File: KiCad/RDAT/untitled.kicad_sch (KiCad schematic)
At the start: 10 parts, among them M1 Fan_4pin

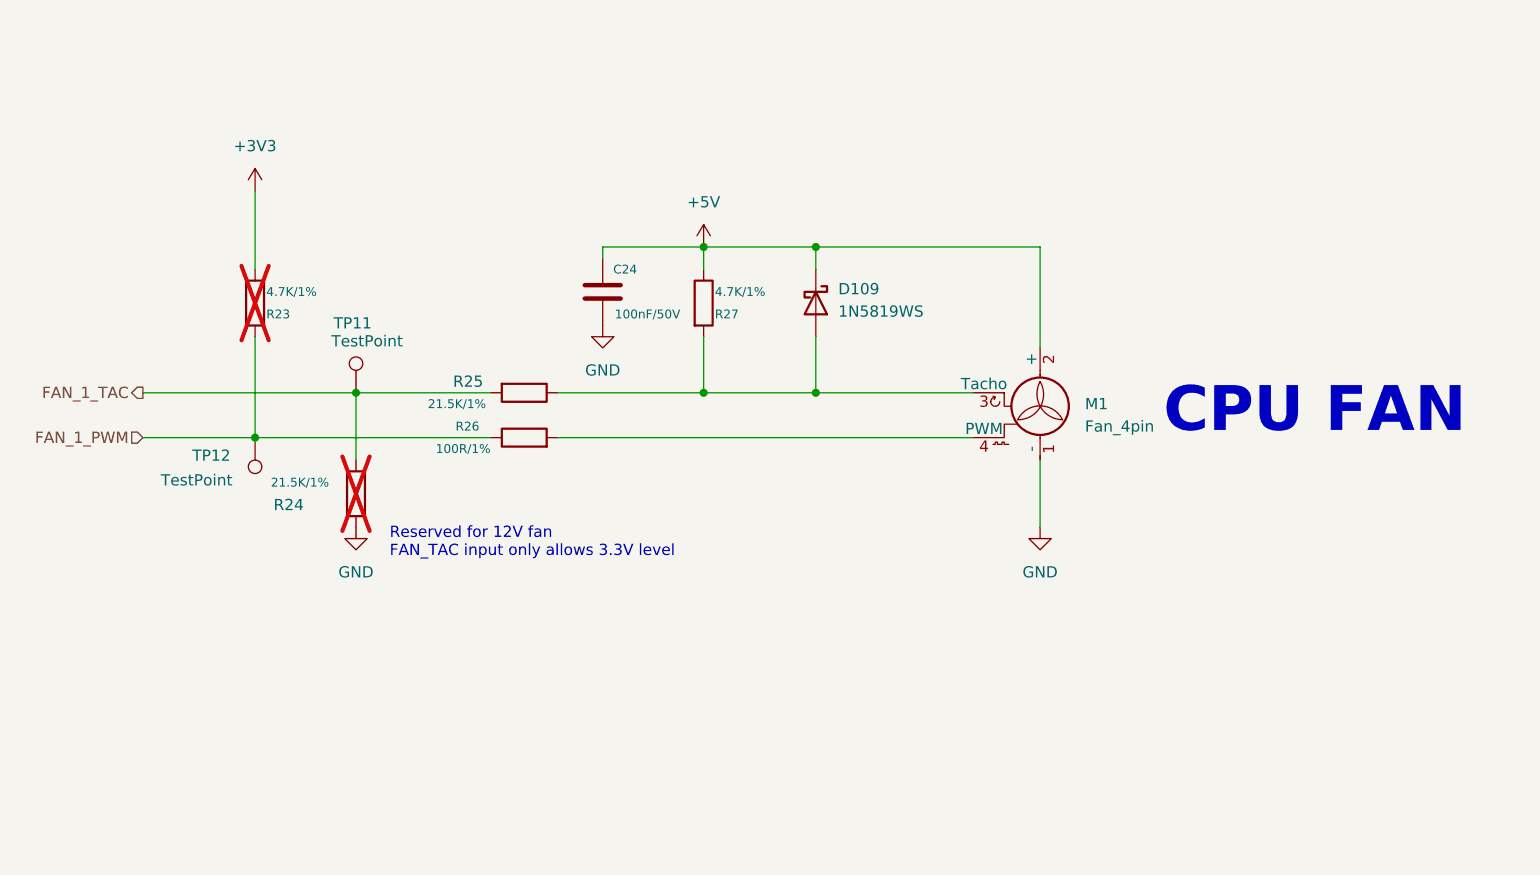
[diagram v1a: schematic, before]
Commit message: Added Libs and DOCS
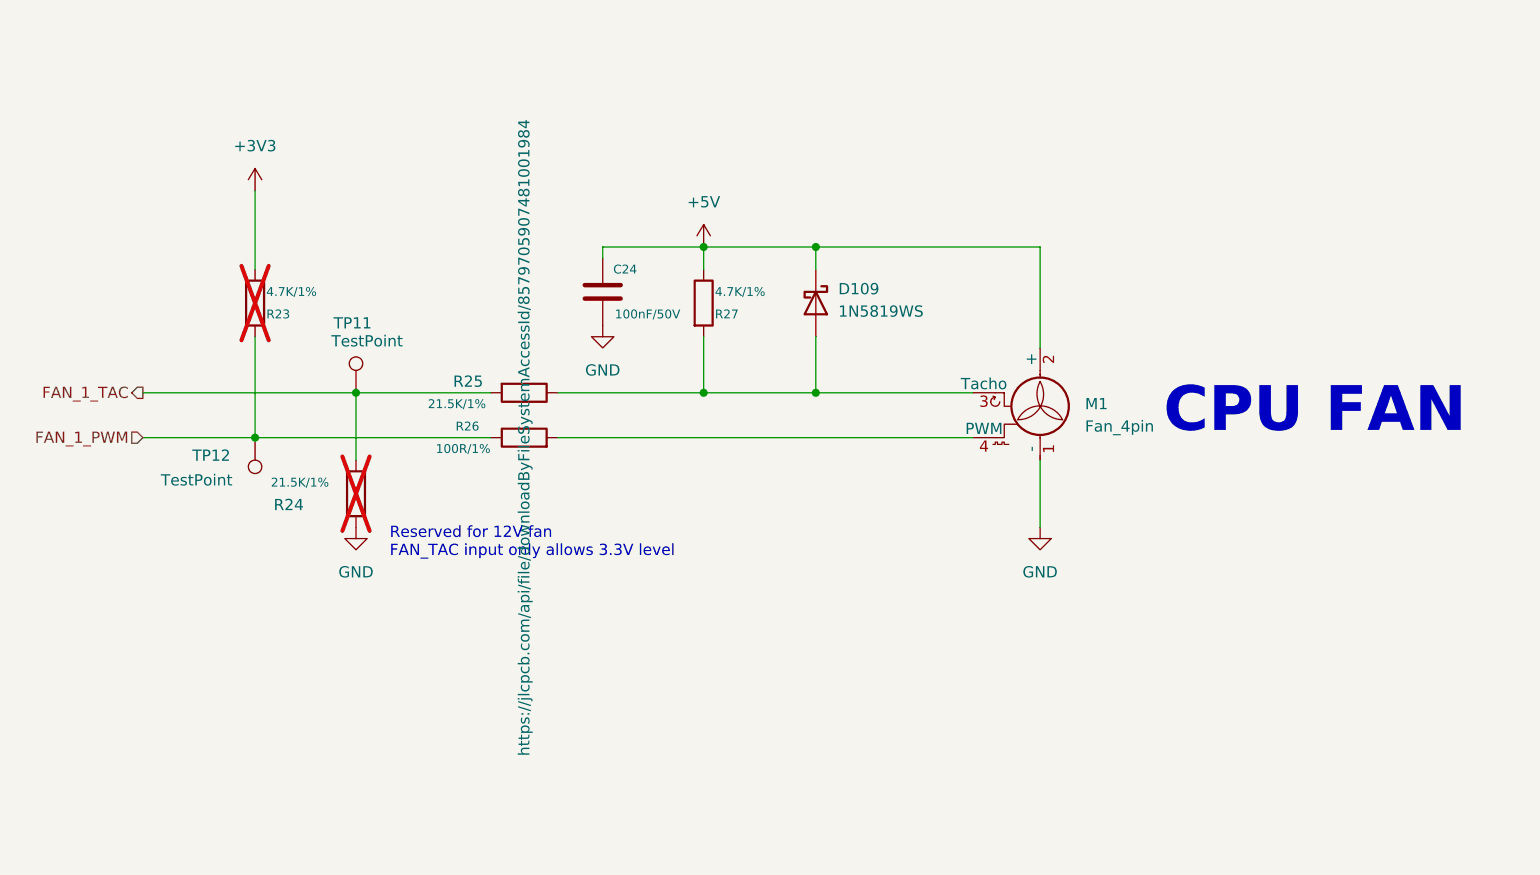
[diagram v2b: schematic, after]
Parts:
- M1: JLCPCB_LINK (none) -> https://jlcpcb.com/partdetail/Jst-B4B_PH_K_K_LF_SN/C5305780
- R26: JLCPCB_LINK (none) -> https://jlcpcb.com/api/file/downloadByFileSystemAccessId/85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
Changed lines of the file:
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@@
 			)
 		)
-		(property "Datasheet" "~"
+		(property "Datasheet" "https://jlcpcb.com/partdetail/25819-0402WGF1000TCE/C25076"
 			(at 139.7 93.98 0)
 			(effects
@@
 			)
 		)
-		(property "JLCPCB_LINK" ""
+		(property "JLCPCB_LINK" "https://jlcpcb.com/api/file/downloadByFileSystemAccessId/8579705907481001984"
 			(at 139.7 93.98 0)
 			(effects
@@
 			)
 		)
-		(property "JLCPCB_LINK" ""
+		(property "JLCPCB_LINK" "https://jlcpcb.com/partdetail/Jst-B4B_PH_K_K_LF_SN/C5305780"
 			(at 198.12 91.44 0)
 			(effects
@@
 					(size 1.27 1.27)
 				)
-			)
-		)
+				(hide yes)
+			)
+		)

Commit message: Sourced and documented all parts
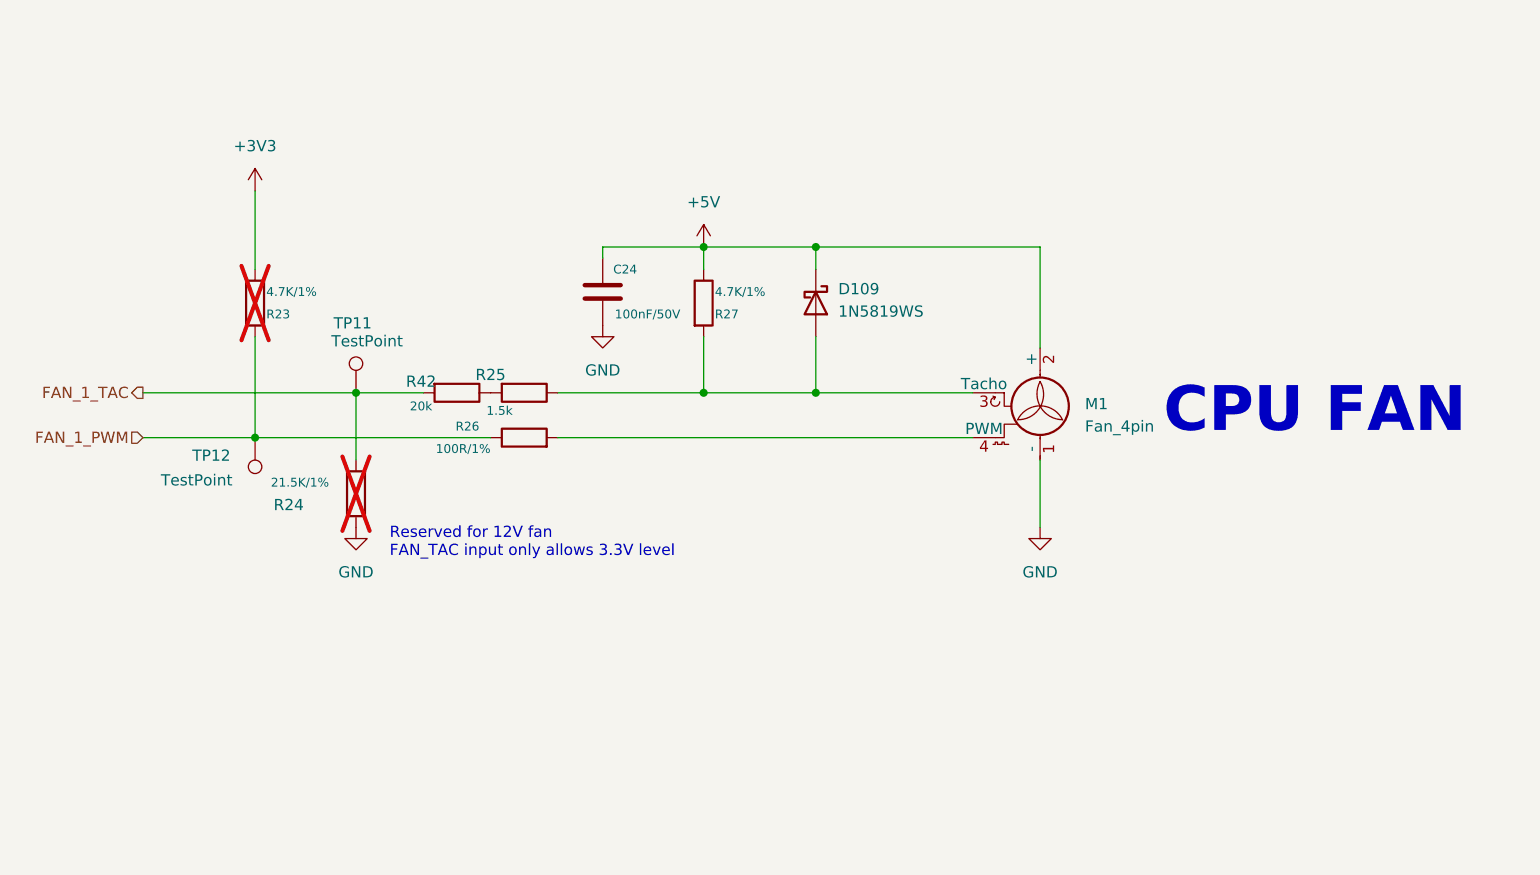
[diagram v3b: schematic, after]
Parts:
- added R42: 20k, A_HDJ_Library:R_0402_1005Metric, symbol Device:R
- C24: JLCPCB_LINK (none) -> https://jlcpcb.com/partdetail/291005-CL05B104KB54PNC/C307331
- D109: JLCPCB_LINK (none) -> https://jlcpcb.com/partdetail/GuangdongHottech-1N5819WS/C19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
- R25: value 21.5K/1% -> 1.5k; JLCPCB_LINK (none) -> https://jlcpcb.com/partdetail/26610-0402WGF1501TCE/C25867
- R26: JLCPCB_LINK https://jlcpcb.com/api/file/downloadByFileSystemAccessId/85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 -> https://jlcpcb.com/partdetail/25819-0402WGF1000TCE/C25076
- R27: JLCPCB_LINK (none) -> https://jlcpcb.com/partdetail/26643-0402WGF4701TCE/C25900
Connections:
- net FAN_1_TAC: now also R42.2; no longer R25.2
- new net: R25.2, R42.1
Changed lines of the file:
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@@
 	(wire
 		(pts
-			(xy 120.65 88.9) (xy 135.89 88.9)
+			(xy 120.65 88.9) (xy 128.27 88.9)
 		)
 		(stroke
@@
 			)
 		)
-		(property "Datasheet" "https://jlcpcb.com/partdetail/25819-0402WGF1000TCE/C25076"
+		(property "Datasheet" "https://jlcpcb.com/api/file/downloadByFileSystemAccessId/8579705907481001984"
 			(at 139.7 93.98 0)
 			(effects
@@
 			)
 		)
-		(property "JLCPCB_LINK" "https://jlcpcb.com/api/file/downloadByFileSystemAccessId/8579705907481001984"
+		(property "JLCPCB_LINK" "https://jlcpcb.com/partdetail/25819-0402WGF1000TCE/C25076"
 			(at 139.7 93.98 0)
 			(effects
@@
 					(size 1.27 1.27)
 				)
+				(hide yes)
 			)
 		)
@@
 			)
 		)
-		(property "Datasheet" "~"
+		(property "Datasheet" "https://jlcpcb.com/api/file/downloadByFileSystemAccessId/8554627388281098240"
 			(at 148.59 77.47 0)
 			(effects
@@
 			)
 		)
-		(property "JLCPCB_LINK" ""
+		(property "JLCPCB_LINK" "https://jlcpcb.com/partdetail/291005-CL05B104KB54PNC/C307331"
 			(at 148.59 77.47 0)
 			(effects
@@
 					(size 1.27 1.27)
 				)
+				(hide yes)
 			)
 		)
@@
 	)
 	(symbol
+		(lib_id "Device:R")
+		(at 132.08 88.9 270)
+		(unit 1)
+		(exclude_from_sim no)
+		(in_bom yes)
+		(on_board yes)
+		(dnp no)
+		(property "Reference" "R42"
+			(at 128.016 87.63 90)
+			(effects
+				(font
+					(size 1.27 1.27)
+				)
+			)
+		)
+		(property "Value" "20k"
+			(at 128.016 90.424 90)
+			(effects
+				(font
+					(size 1 1)
+				)
+			)
+		)
+		(property "Footprint" "A_HDJ_Library:R_0402_1005Metric"
+			(at 132.08 87.122 90)
+			(effects
+				(font
+					(size 1.27 1.27)
+				)
+				(hide yes)
+			)
+		)
+		(property "Datasheet" "https://jlcpcb.com/api/file/downloadByFileSystemAccessId/8579705988980932608"
+			(at 132.08 88.9 0)
+			(effects
+				(font
+					(size 1.27 1.27)
+				)
+				(hide yes)
+			)
+		)
+		(property "Description" ""
+			(at 132.08 88.9 0)
+			(effects
+				(font
+					(size 1.27 1.27)
+				)
+				(hide yes)
+			)
+		)
+		(property "SCH_Show_Footprint" ""
+			(at 132.08 88.9 0)
+			(effects
+				(font
+					(size 1.27 1.27)
+				)
+				(hide yes)
+			)
+		)
+		(property "Sim.Device" ""
+			(at 132.08 88.9 0)
+			(effects
+				(font
+					(size 1.27 1.27)
+				)
+				(hide yes)
+			)
+		)
+		(property "Sim.Pins" ""
+			(at 132.08 88.9 0)
+			(effects
+				(font
+					(size 1.27 1.27)
+				)
+				(hide yes)
+			)
+		)
+		(property "Sim.Type" ""
+			(at 132.08 88.9 0)
+			(effects
+				(font
+					(size 1.27 1.27)
+				)
+				(hide yes)
+			)
+		)
+		(property "JLCPCB_LINK" "https://jlcpcb.com/partdetail/26508-0402WGF2002TCE/C25765"
+			(at 132.08 88.9 0)
+			(effects
+				(font
+					(size 1.27 1.27)
+				)
+				(hide yes)
+			)
+		)
+		(pin "1"
+		)
+		(pin "2"
+		)
+		(instances
+			(project "RDAT"
+				(path "/0db9370a-8a21-4fd2-83a9-f207c3725dc9/2f5ffc1e-d25d-4ef5-8610-5326cc58210f"
+					(reference "R42")
+					(unit 1)
+				)
+			)
+		)
+	)
+	(symbol
 		(lib_id "power:+5V")
 		(at 160.02 72.39 0)
@@
 		(dnp no)
 		(property "Reference" "R25"
-			(at 133.35 87.63 90)
-			(effects
-				(font
-					(size 1.27 1.27)
-				)
-			)
-		)
-		(property "Value" "21.5K/1%"
-			(at 132.08 90.17 90)
+			(at 135.89 86.868 90)
+			(effects
+				(font
+					(size 1.27 1.27)
+				)
+			)
+		)
+		(property "Value" "1.5k"
+			(at 136.906 90.932 90)
 			(effects
 				(font
@@
 			)
 		)
-		(property "Datasheet" "~"
+		(property "Datasheet" "https://jlcpcb.com/api/file/downloadByFileSystemAccessId/8579705932919590912"
 			(at 139.7 88.9 0)
 			(effects
@@
 			)
 		)
-		(property "JLCPCB_LINK" ""
+		(property "JLCPCB_LINK" "https://jlcpcb.com/partdetail/26610-0402WGF1501TCE/C25867"
 			(at 139.7 88.9 0)
 			(effects
@@
 					(size 1.27 1.27)
 				)
+				(hide yes)
 			)
 		)
@@
 			)
 		)
-		(property "Datasheet" "https://datasheet.lcsc.com/lcsc/2204281430_Guangdong-Hottech-1N5819WS_C191023.pdf"
+		(property "Datasheet" "https://jlcpcb.com/api/file/downloadByFileSystemAccessId/8550723919347523584"
 			(at 172.72 78.74 0)
 			(effects
@@
 			)
 		)
-		(property "JLCPCB_LINK" ""
+		(property "JLCPCB_LINK" "https://jlcpcb.com/partdetail/GuangdongHottech-1N5819WS/C191023"
 			(at 172.72 78.74 0)
 			(effects
@@
 					(size 1.27 1.27)
 				)
+				(hide yes)
 			)
 		)
@@
 			)
 		)
-		(property "Datasheet" "~"
+		(property "Datasheet" "https://jlcpcb.com/api/file/downloadByFileSystemAccessId/8579705941367193600"
 			(at 160.02 78.74 0)
 			(effects
@@
 			)
 		)
-		(property "JLCPCB_LINK" ""
+		(property "JLCPCB_LINK" "https://jlcpcb.com/partdetail/26643-0402WGF4701TCE/C25900"
 			(at 160.02 78.74 0)
 			(effects
@@
 					(size 1.27 1.27)
 				)
-			)
-		)
+				(hide yes)
+			)
+		)

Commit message: Push before Board Layout
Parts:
- C24: footprint A_HDJ_Library:C_0402_1005Metric -> Capacitor_SMD:C_0402_1005Metric
- D109: footprint A_HDJ_Library:D_SOD-323 -> Diode_SMD:D_SOD-323
- M1: footprint A_HDJ_Library:JST_PH_B4B-PH-K_1x04_P2.00mm_Vertical -> footprints:JST_B4B-PH-SM4-TBT_LF__SN_
- R25, R26, R27, R42: footprint A_HDJ_Library:R_0402_1005Metric -> Resistor_SMD:R_0402_1005Metric
- TP11, TP12: footprint A_HDJ_Library:TestPoint_Pad_D1.5mm -> TestPoint:TestPoint_Pad_D1.0mm
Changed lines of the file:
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@@
 			)
 		)
-		(property "Footprint" "A_HDJ_Library:R_0402_1005Metric"
+		(property "Footprint" "Resistor_SMD:R_0402_1005Metric"
 			(at 139.7 95.758 90)
 			(effects
@@
 			)
 		)
-		(property "Footprint" "A_HDJ_Library:C_0402_1005Metric"
+		(property "Footprint" "Capacitor_SMD:C_0402_1005Metric"
 			(at 149.5552 81.28 0)
 			(effects
@@
 			)
 		)
-		(property "Footprint" "A_HDJ_Library:TestPoint_Pad_D1.5mm"
+		(property "Footprint" "TestPoint:TestPoint_Pad_D1.0mm"
 			(at 104.14 93.98 0)
 			(effects
@@
 			)
 		)
-		(property "Footprint" "A_HDJ_Library:R_0402_1005Metric"
+		(property "Footprint" "Resistor_SMD:R_0402_1005Metric"
 			(at 132.08 87.122 90)
 			(effects
@@
 			)
 		)
-		(property "Footprint" "A_HDJ_Library:JST_PH_B4B-PH-K_1x04_P2.00mm_Vertical"
+		(property "Footprint" "footprints:JST_B4B-PH-SM4-TBT_LF__SN_"
 			(at 198.12 91.186 0)
 			(effects
@@
 			)
 		)
-		(property "Footprint" "A_HDJ_Library:R_0402_1005Metric"
+		(property "Footprint" "Resistor_SMD:R_0402_1005Metric"
 			(at 139.7 87.122 90)
 			(effects
@@
 			)
 		)
-		(property "Footprint" "A_HDJ_Library:D_SOD-323"
+		(property "Footprint" "Diode_SMD:D_SOD-323"
 			(at 168.275 78.74 0)
 			(effects
@@
 			)
 		)
-		(property "Footprint" "A_HDJ_Library:R_0402_1005Metric"
+		(property "Footprint" "Resistor_SMD:R_0402_1005Metric"
 			(at 158.242 78.74 90)
 			(effects
@@
 			)
 		)
-		(property "Footprint" "A_HDJ_Library:TestPoint_Pad_D1.5mm"
+		(property "Footprint" "TestPoint:TestPoint_Pad_D1.0mm"
 			(at 125.73 88.9 0)
 			(effects

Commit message: End Of day commit
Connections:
- net GND: now also M1.SH1 (Sheild), M1.SH2 (Sheild)
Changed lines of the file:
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@@
+	)
+	(junction
+		(at 198.12 96.52)
+		(diameter 0)
+		(color 0 0 0 0)
 	)
 	(junction
@@
 	(wire
 		(pts
+			(xy 212.09 86.36) (xy 212.09 96.52)
+		)
+		(stroke
+			(width 0)
+			(type default)
+		)
+	)
+	(wire
+		(pts
 			(xy 96.52 93.98) (xy 109.22 93.98)
 		)
@@
 	(wire
 		(pts
+			(xy 205.74 86.36) (xy 212.09 86.36)
+		)
+		(stroke
+			(width 0)
+			(type default)
+		)
+	)
+	(wire
+		(pts
 			(xy 143.51 93.98) (xy 190.5 93.98)
+		)
+		(stroke
+			(width 0)
+			(type default)
+		)
+	)
+	(wire
+		(pts
+			(xy 198.12 96.52) (xy 212.09 96.52)
 		)
 		(stroke
@@
 		(pin "4"
 		)
+		(pin "SH1"
+		)
+		(pin "SH2"
+		)
 		(instances

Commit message: 2x checing of bom on JLCPCB
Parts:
- C24: value 100nF/50V -> 100nF
- R26: value 100R/1% -> 100R
- R27: value 4.7K/1% -> 4.7K
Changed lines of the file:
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@@
 			)
 		)
-		(property "Value" "100R/1%"
+		(property "Value" "100R"
 			(at 135.89 95.25 90)
 			(effects
@@
 				)
 				(hide yes)
+			)
+		)
+		(property "JLCPCB_PART_NUMBER" ""
+			(at 139.7 93.98 0)
+			(effects
+				(font
+					(size 1.27 1.27)
+				)
 			)
 		)
@@
 			)
 		)
+		(property "JLCPCB_PART_NUMBER" ""
+			(at 120.65 100.33 0)
+			(effects
+				(font
+					(size 1.27 1.27)
+				)
+			)
+		)
 		(pin "1"
 		)
@@
 			)
 		)
-		(property "Value" "100nF/50V"
+		(property "Value" "100nF"
 			(at 153.67 80.01 0)
 			(effects
@@
 				)
 				(hide yes)
+			)
+		)
+		(property "JLCPCB_PART_NUMBER" ""
+			(at 148.59 77.47 0)
+			(effects
+				(font
+					(size 1.27 1.27)
+				)
 			)
 		)
@@
 		)
 		(property "JLCPCB_LINK" ""
+			(at 109.22 93.98 0)
+			(effects
+				(font
+					(size 1.27 1.27)
+				)
+			)
+		)
+		(property "JLCPCB_PART_NUMBER" ""
 			(at 109.22 93.98 0)
 			(effects
@@
 			)
 		)
+		(property "JLCPCB_PART_NUMBER" ""
+			(at 132.08 88.9 0)
+			(effects
+				(font
+					(size 1.27 1.27)
+				)
+			)
+		)
 		(pin "1"
 		)
@@
 			)
 		)
+		(property "JLCPCB_PART_NUMBER" ""
+			(at 109.22 78.74 0)
+			(effects
+				(font
+					(size 1.27 1.27)
+				)
+			)
+		)
 		(pin "1"
 		)
@@
 			)
 		)
+		(property "JLCPCB_PART_NUMBER" ""
+			(at 198.12 91.44 0)
+			(effects
+				(font
+					(size 1.27 1.27)
+				)
+			)
+		)
 		(pin "1"
 		)
@@
 				)
 				(hide yes)
+			)
+		)
+		(property "JLCPCB_PART_NUMBER" ""
+			(at 139.7 88.9 0)
+			(effects
+				(font
+					(size 1.27 1.27)
+				)
 			)
 		)
@@
 			)
 		)
+		(property "JLCPCB_PART_NUMBER" ""
+			(at 172.72 78.74 0)
+			(effects
+				(font
+					(size 1.27 1.27)
+				)
+			)
+		)
 		(pin "1"
 		)
@@
 			)
 		)
-		(property "Value" "4.7K/1%"
+		(property "Value" "4.7K"
 			(at 161.29 77.47 0)
 			(effects
@@
 				)
 				(hide yes)
+			)
+		)
+		(property "JLCPCB_PART_NUMBER" ""
+			(at 160.02 78.74 0)
+			(effects
+				(font
+					(size 1.27 1.27)
+				)
 			)
 		)
@@
 			(at 120.65 88.9 0)
 			(effects
+				(font
+					(size 1.27 1.27)
+				)
+			)
+		)
+		(property "JLCPCB_PART_NUMBER" ""
+			(at 120.65 88.9 0)
+			(effects
